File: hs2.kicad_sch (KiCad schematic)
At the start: 55 parts

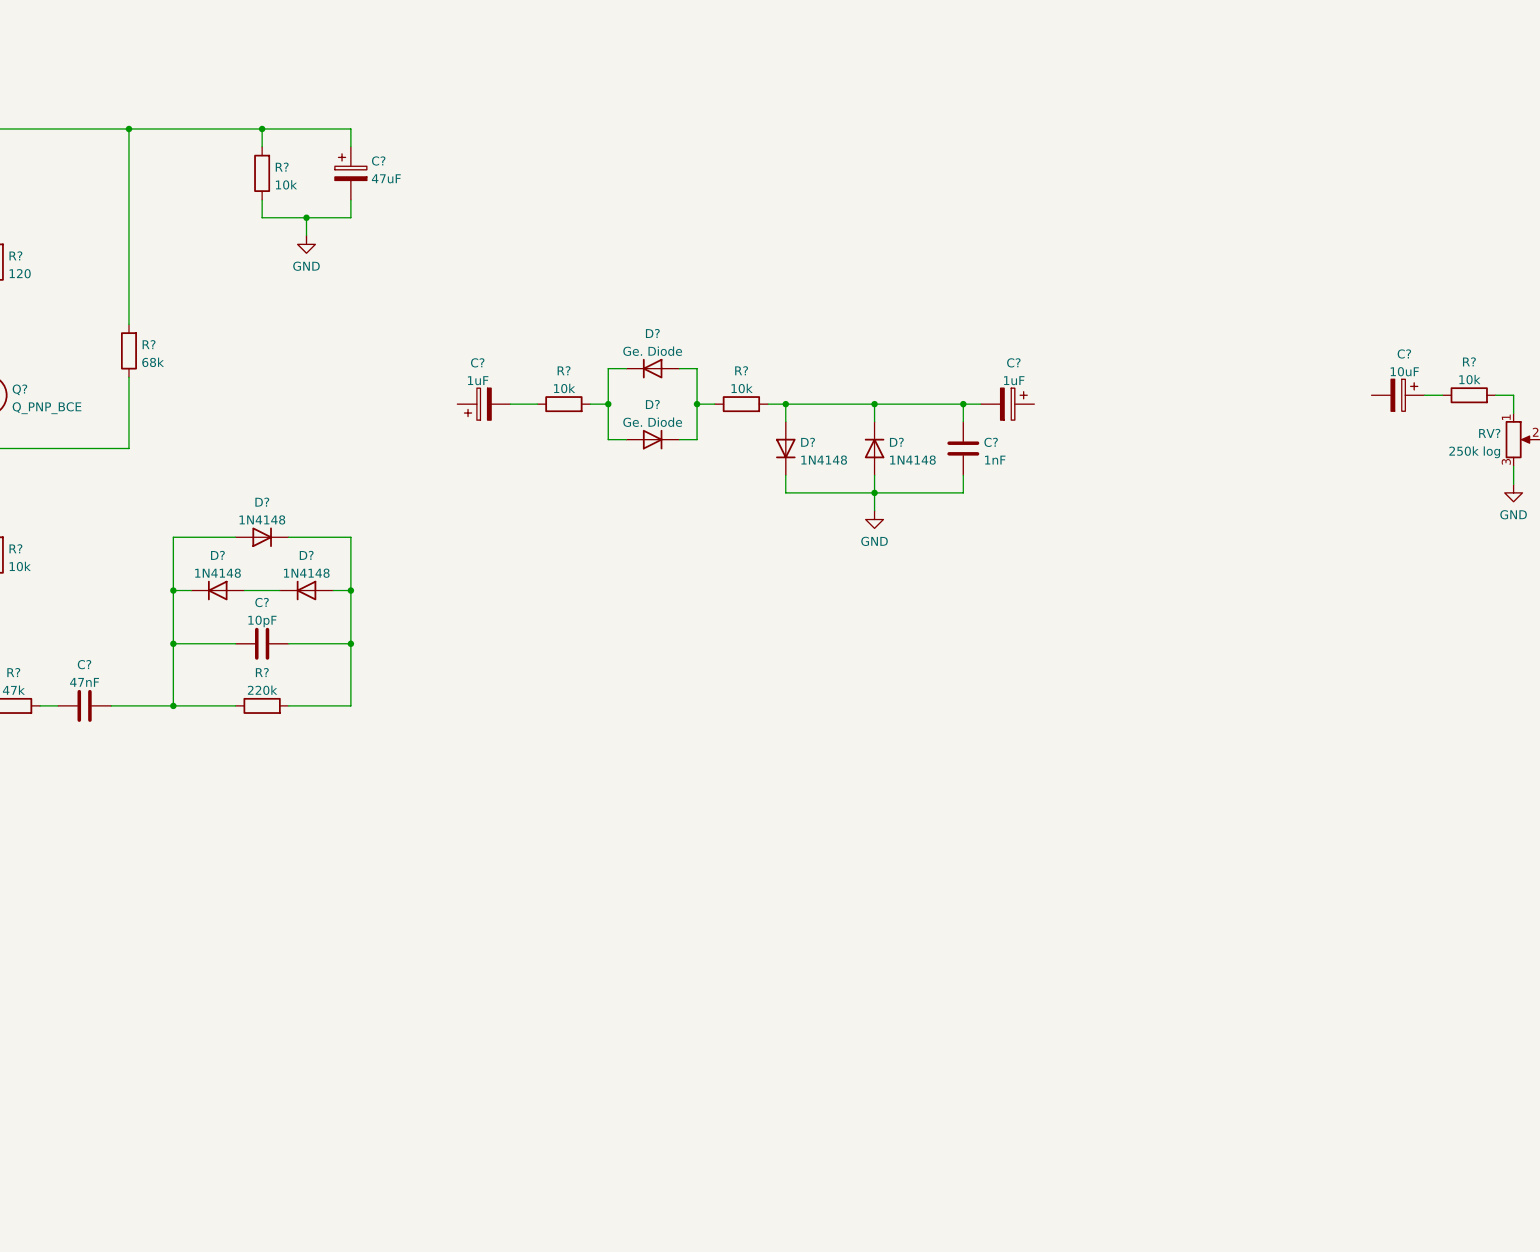
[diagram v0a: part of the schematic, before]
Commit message: Renaming the project
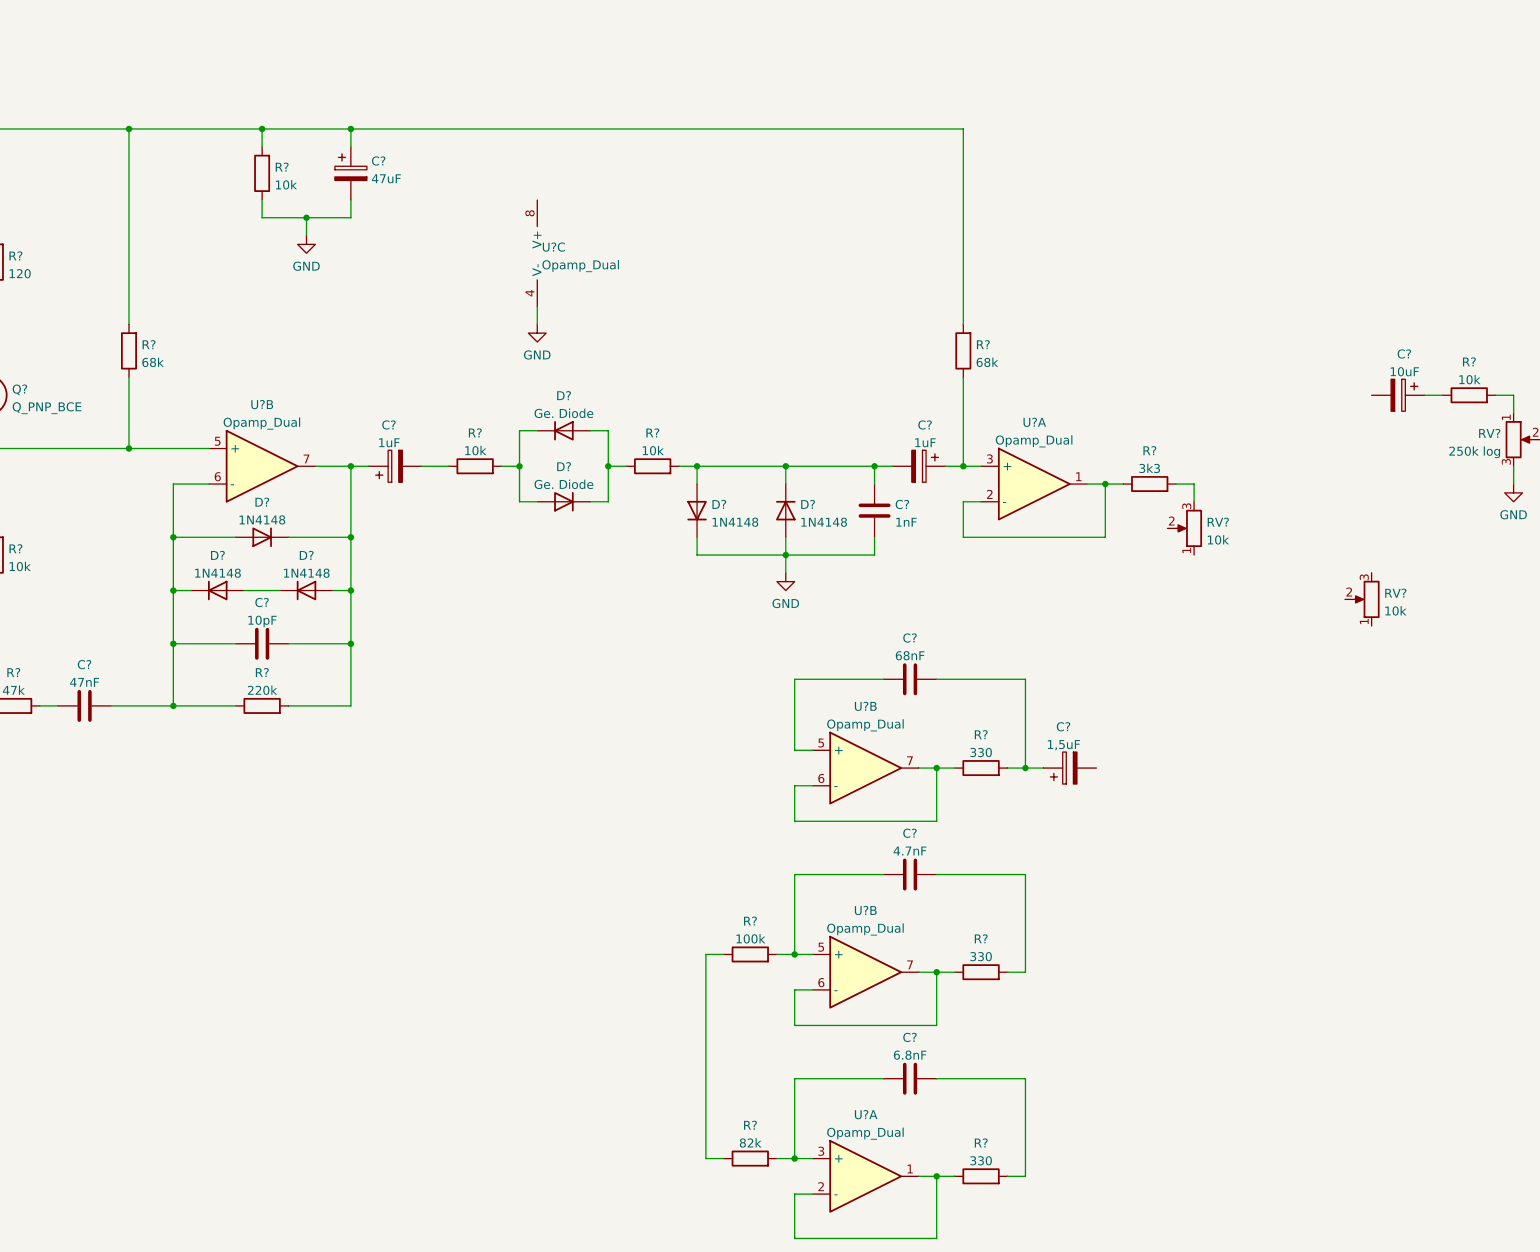
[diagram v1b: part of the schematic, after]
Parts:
- added C?: 68nF, symbol Device:C
- added C?: 1,5uF, symbol Device:C_Polarized
- added C?: 6.8nF, symbol Device:C
- added C?: 4.7nF, symbol Device:C
- added R? (x3): 330, symbol Device:R
- added R?: 3k3, symbol Device:R
- added R?: 82k, symbol Device:R
- added R?: 100k, symbol Device:R
- added R?: 68k, symbol Device:R
- added RV? (x2): 10k, symbol Device:R_Potentiometer
- added U? (x6): Opamp_Dual, symbol Device:Opamp_Dual
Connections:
- net GND: now also U?.4 (V-)
- net at C?.2, D?.1 (K), D?.2 (A)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: now also C?.1, U?.7
- net at C?.1, R?.2, R?.2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: now also R?.2
- net at C?.1, C?.2, D?.1 (K)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: now also U?.6 (-)
- net at C?.2, Q?.2 (C), R?.1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: now also U?.5 (+)
- net at C?.1: now also R?.1, U?.3 (+)
- new net: C?.1, U?.5 (+)
- new net: C?.1, C?.2, R?.2
- new net: C?.1, R?.2, U?.5 (+)
- new net: R?.1, U?.6 (-), U?.7 (x2)
- new net: R?.1, U?.1, U?.2 (-) (x2)
- new net: C?.2, R?.2 (x2)
- new net: R?.2, RV?.3
- new net: R?.1, R?.1
- new net: C?.1, R?.2, U?.3 (+)
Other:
- title: Boss HM-2 -> HS2
- moved on the sheet: C?, D?, R?

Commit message: schematics: Drawing the circuit
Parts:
- removed C?: 68nF, symbol Device:C
- removed C?: 1nF, symbol Device:C
- removed C?: 1,5uF, symbol Device:C_Polarized
- removed C? (x3): 47uF, symbol Device:C_Polarized
- removed C?: 47nF, symbol Device:C
- removed C?: 6.8nF, symbol Device:C
- removed C?: 10uF, symbol Device:C_Polarized
- removed C?: 10pF, symbol Device:C
- removed C?: 4.7nF, symbol Device:C
- removed C? (x2): 1uF, symbol Device:C_Polarized
- removed D? (x5): 1N4148, Diode_THT:D_DO-35_SOD27_P7.62mm_Horizontal, symbol Diode:1N4148
- removed D? (x2): Ge. Diode, symbol Device:D
- removed J?: Conn_01x01, symbol Connector_Generic:Conn_01x01
- removed R? (x3): 330, symbol Device:R
- removed R?: 3k3, symbol Device:R
- removed R?: 82k, symbol Device:R
- removed R?: 1k, symbol Device:R
- removed R? (x2): 68k, symbol Device:R
- removed R?: 150, symbol Device:R
- removed R? (x5): 10k, symbol Device:R
- removed R?: 100k, symbol Device:R
- removed R?: 220k, symbol Device:R
- removed R?: 47k, symbol Device:R
- removed RV? (x2): 10k, symbol Device:R_Potentiometer
- removed RV? (x2): 250k log, symbol Device:R_Potentiometer
- removed U? (x6): Opamp_Dual, symbol Device:Opamp_Dual
- added C?: 47uF, symbol Device:C_Polarized
- added C?: 47n, symbol Device:C
- added C? (x3): 1uF, symbol Device:C_Polarized
- added C?: 47nF, symbol Device:C
- added C?: 1nF, symbol Device:C
- added C?: 150nF, symbol Device:C
- added C?: 470p, symbol Device:C
- added C?: 4.7nF, symbol Device:C
- added C?: 68nF, symbol Device:C
- added C?: 100nF, symbol Device:C
- added C? (x3): 10uF, symbol Device:C_Polarized
- added C?: 100pF, symbol Device:C
- added C?: 6.8nF, symbol Device:C
- added C?: 1.5uF, symbol Device:C_Polarized
- added C?: 100uF, symbol Device:C_Polarized
- added D? (x5): 1N4148, Diode_THT:D_DO-35_SOD27_P7.62mm_Horizontal, symbol Diode:1N4148
- added D?: 1N4001, Diode_THT:D_DO-41_SOD81_P10.16mm_Horizontal, symbol Diode:1N4001
- added D? (x2): DIODE, symbol pspice:DIODE
- added J?: Conn_01x01, symbol Connector_Generic:Conn_01x01
- added R? (x2): 68k, symbol Device:R
- added R?: 470k, symbol Device:R
- added R? (x6): 10k, symbol Device:R
- added R? (x2): 3k3, symbol Device:R
- added R? (x2): 1k, symbol Device:R
- added R? (x3): 100k, symbol Device:R
- added R?: 82k, symbol Device:R
- added R?: 47k, symbol Device:R
- added R? (x4): 330, symbol Device:R
- added R?: 220k, symbol Device:R
- added R?: 150, symbol Device:R
- added RV?: A10k, symbol Device:R_Potentiometer
- added RV? (x2): B50k, symbol Device:R_Potentiometer
- added RV?: C250k, symbol Device:R_Potentiometer
- added U? (x9): Opamp_Dual, symbol Device:Opamp_Dual
- C?: value 47nF -> 100pF
- C?: value 10pF -> 100pF
- R?: value 100k -> 470k
- R?: value 10k -> 22k
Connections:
- net +9V: now also R?.2, R?.2, R?.2, U?.8 (V+), U?.8 (V+), U?.8 (V+)
- net GND: now also C?.2, C?.2, C?.2, C?.2, D?.1 (K), D?.2 (A), D?.2 (A), R?.1, R?.1, R?.1, RV?.1, RV?.2, U?.4 (V-), U?.4 (V-), U?.4 (V-)
- net at C?.1, C?.2, Q?.2 (C)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: now also R?.2
- net at R?.2, R?.2, R?.2: now also C?.1, R?.1
- net 1/2V: now reaches R?.2
- net 1/2V: now also C?.1, R?.1, R?.1, R?.1, R?.1, R?.1, R?.2, R?.2
- net at C?.2, Q?.2 (C), R?.2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: now also R?.1, U?.3 (+)
- new net: R?.2, RV?.3
- new net: C?.2, R?.2
- new net: C?.1, R?.2 (x2)
- new net: C?.2, J?.1 (Pin_1), R?.2
- new net: RV?.1, RV?.1, U?.5 (+)
- new net: C?.1, R?.1, RV?.3, RV?.3, U?.6 (-)
- new net: C?.1, C?.2, R?.2, U?.7
- new net: C?.1, C?.2, D?.1 (K), D?.2 (A), R?.1, U?.2 (-)
- new net: D?.1 (K), D?.2 (A)
- new net: C?.1, R?.2, U?.5 (+)
- new net: C?.1, C?.2, D?.1 (K), D?.2 (A), R?.2
- new net: R?.1, U?.1, U?.2 (-)
- new net: C?.2, R?.2, U?.3 (+)
- new net: D?.1 (K), D?.2 (A), R?.1
- new net: C?.2, R?.1 (x2)
- new net: R?.2, U?.6 (-), U?.7
- new net: C?.1, C?.1, RV?.2
- new net: C?.1, C?.2, R?.2 (x2)
- new net: C?.2, R?.2, U?.2 (-)
- new net: C?.1, C?.2, D?.1 (K), D?.2 (A), R?.2, U?.1
- new net: C?.1, C?.1, R?.2
- new net: C?.1, D?.1 (K), R?.1, R?.1
- new net: C?.2, RV?.2
- new net: R?.1, R?.2
- new net: C?.2, R?.2, U?.6 (-)
- new net: R?.1, RV?.3
- new net: R?.1, U?.1, U?.3 (+)
- new net: C?.2, RV?.1
- new net: C?.1, R?.1
- new net: D?.1 (K), D?.2 (A), R?.2
- new net: R?.1, U?.5 (+), U?.7
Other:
- moved on the sheet: C?, Q?, R?

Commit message: schematics: First version of the schematics
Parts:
- removed Q?: 2SC2240, Package_TO_SOT_THT:TO-92_Inline, symbol Transistor_BJT:2SC1815
- removed Q?: Q_PNP_BCE, symbol Device:Q_PNP_BCE
- added Q2, Q4: 2N3904, Package_TO_SOT_THT:TO-92_Inline, symbol Transistor_BJT:2N3904
- added Q3: 2N3906, Package_TO_SOT_THT:TO-92_Inline, symbol Transistor_BJT:2N3906
- Q1: renamed from Q?; value BF245A -> 2N5457
- gave numbers to parts that had none: 82
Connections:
- net +9V: now also Q4.3 (C)
- net at RV4.2: now also C23.1
- net at C23.2, R34.2: now also Q4.2 (B)
- net at RV2.1, RV3.1, U3.5 (+): now also R30.1
- net at R12.2: now also Q2.1 (E)
- net at C6.2, C8.1, R11.1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: now also Q2.3 (C)
- net at C6.1, R7.2, R8.2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: now also Q2.2 (B)
- net at C10.2, R17.2, R19.2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: now also Q3.1 (E)
- net at C10.1, R14.2, R16.1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: now also Q3.2 (B)
- net at C21.2, R31.2: now also U3.3 (+); no longer U3.2 (-)
- net at R35.2, R36.1: now also Q4.1 (E)
- net at C18.2, R26.2: now also U1.5 (+); no longer U1.6 (-)
- net at R32.1, U3.1: now also U3.2 (-); no longer U3.3 (+)
- net at R18.1: now also Q3.3 (C)
- net at R28.1, U1.7: now also U1.6 (-); no longer U1.5 (+)
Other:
- moved on the sheet: C1, C10, C11, C12, C13, C14, C15, C16, C17, C18, C19, C20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

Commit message: Updating the designators and initial footprint assignment
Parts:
- D5, D6: footprint (none) -> Diode_THT:D_DO-41_SOD81_P10.16mm_Horizontal
- H1, H2, H3, H4: footprint (none) -> MountingHole:MountingHole_3.2mm_M3_Pad_TopBottom
- J1, J2: footprint (none) -> Connector_PinHeader_2.54mm:PinHeader_1x01_P2.54mm_Vertical
- R1, R4: footprint (none) -> Resistor_THT:R_Axial_DIN0207_L6.3mm_D2.5mm_P10.16mm_Horizontal
- R10: renamed from R11; footprint (none) -> Resistor_THT:R_Axial_DIN0207_L6.3mm_D2.5mm_P10.16mm_Horizontal
- R11: renamed from R14; footprint (none) -> Resistor_THT:R_Axial_DIN0207_L6.3mm_D2.5mm_P10.16mm_Horizontal
- R12: renamed from R16; footprint (none) -> Resistor_THT:R_Axial_DIN0207_L6.3mm_D2.5mm_P10.16mm_Horizontal
- R13: renamed from R17; footprint (none) -> Resistor_THT:R_Axial_DIN0207_L6.3mm_D2.5mm_P10.16mm_Horizontal
- R14: renamed from R19; footprint (none) -> Resistor_THT:R_Axial_DIN0207_L6.3mm_D2.5mm_P10.16mm_Horizontal
- R15: renamed from R18; footprint (none) -> Resistor_THT:R_Axial_DIN0207_L6.3mm_D2.5mm_P10.16mm_Horizontal
- R16: renamed from R20; footprint (none) -> Resistor_THT:R_Axial_DIN0207_L6.3mm_D2.5mm_P10.16mm_Horizontal
- R17: renamed from R15; footprint (none) -> Resistor_THT:R_Axial_DIN0207_L6.3mm_D2.5mm_P10.16mm_Horizontal
- R18: renamed from R21; footprint (none) -> Resistor_THT:R_Axial_DIN0207_L6.3mm_D2.5mm_P10.16mm_Horizontal
- R19: renamed from R22; footprint (none) -> Resistor_THT:R_Axial_DIN0207_L6.3mm_D2.5mm_P10.16mm_Horizontal
- R2: renamed from R3; footprint (none) -> Resistor_THT:R_Axial_DIN0207_L6.3mm_D2.5mm_P10.16mm_Horizontal
- R20: renamed from R23; footprint (none) -> Resistor_THT:R_Axial_DIN0207_L6.3mm_D2.5mm_P10.16mm_Horizontal
- R21: renamed from R27; footprint (none) -> Resistor_THT:R_Axial_DIN0207_L6.3mm_D2.5mm_P10.16mm_Horizontal
- R22: renamed from R30; footprint (none) -> Resistor_THT:R_Axial_DIN0207_L6.3mm_D2.5mm_P10.16mm_Horizontal
- R23: renamed from R29; footprint (none) -> Resistor_THT:R_Axial_DIN0207_L6.3mm_D2.5mm_P10.16mm_Horizontal
- R24: renamed from R33; footprint (none) -> Resistor_THT:R_Axial_DIN0207_L6.3mm_D2.5mm_P10.16mm_Horizontal
- R25: renamed from R34; footprint (none) -> Resistor_THT:R_Axial_DIN0207_L6.3mm_D2.5mm_P10.16mm_Horizontal
- R26: renamed from R35; footprint (none) -> Resistor_THT:R_Axial_DIN0207_L6.3mm_D2.5mm_P10.16mm_Horizontal
- R27: renamed from R36; footprint (none) -> Resistor_THT:R_Axial_DIN0207_L6.3mm_D2.5mm_P10.16mm_Horizontal
- R28: renamed from R37; footprint (none) -> Resistor_THT:R_Axial_DIN0207_L6.3mm_D2.5mm_P10.16mm_Horizontal
- R29: renamed from R24; footprint (none) -> Resistor_THT:R_Axial_DIN0207_L6.3mm_D2.5mm_P10.16mm_Horizontal
- R3: renamed from R7; footprint (none) -> Resistor_THT:R_Axial_DIN0207_L6.3mm_D2.5mm_P10.16mm_Horizontal
- R30: renamed from R25; footprint (none) -> Resistor_THT:R_Axial_DIN0207_L6.3mm_D2.5mm_P10.16mm_Horizontal
- R31: renamed from R26; footprint (none) -> Resistor_THT:R_Axial_DIN0207_L6.3mm_D2.5mm_P10.16mm_Horizontal
- R32: renamed from R28; footprint (none) -> Resistor_THT:R_Axial_DIN0207_L6.3mm_D2.5mm_P10.16mm_Horizontal
- R33: renamed from R31; footprint (none) -> Resistor_THT:R_Axial_DIN0207_L6.3mm_D2.5mm_P10.16mm_Horizontal
- R34: renamed from R32; footprint (none) -> Resistor_THT:R_Axial_DIN0207_L6.3mm_D2.5mm_P10.16mm_Horizontal
- R35: renamed from R5; footprint (none) -> Resistor_THT:R_Axial_DIN0207_L6.3mm_D2.5mm_P10.16mm_Horizontal
- R36: renamed from R6; footprint (none) -> Resistor_THT:R_Axial_DIN0207_L6.3mm_D2.5mm_P10.16mm_Horizontal
- R38: renamed from R2; footprint (none) -> Resistor_THT:R_Axial_DIN0207_L6.3mm_D2.5mm_P10.16mm_Horizontal
- R5: renamed from R8; footprint (none) -> Resistor_THT:R_Axial_DIN0207_L6.3mm_D2.5mm_P10.16mm_Horizontal
- R6: renamed from R9; footprint (none) -> Resistor_THT:R_Axial_DIN0207_L6.3mm_D2.5mm_P10.16mm_Horizontal
- R7: renamed from R12; footprint (none) -> Resistor_THT:R_Axial_DIN0207_L6.3mm_D2.5mm_P10.16mm_Horizontal
- R8: renamed from R13; footprint (none) -> Resistor_THT:R_Axial_DIN0207_L6.3mm_D2.5mm_P10.16mm_Horizontal
- R9: renamed from R10; footprint (none) -> Resistor_THT:R_Axial_DIN0207_L6.3mm_D2.5mm_P10.16mm_Horizontal
- U1, U2, U3: footprint (none) -> Package_SIP:SIP-8_19x3mm_P2.54mm
- VR1: renamed from RV1; footprint (none) -> TerminalBlock:TerminalBlock_bornier-3_P5.08mm
- VR2: renamed from RV2; footprint (none) -> TerminalBlock:TerminalBlock_bornier-3_P5.08mm
- VR3: renamed from RV3; footprint (none) -> TerminalBlock:TerminalBlock_bornier-3_P5.08mm
- VR4: renamed from RV4; footprint (none) -> TerminalBlock:TerminalBlock_bornier-3_P5.08mm
- renumbered C12 to C10, C15 to C11, C16 to C12, C19 to C13, C13 to C14, C17 to C15, C20 to C16, C14 to C17, C21 to C19, C3 to C2, C22 to C20, C23 to C21, C24 to C22, C2 to C23, C4 to C24, C6 to C3, C5 to C4, C7 to C5, C8 to C6, C10 to C7, C9 to C8, C11 to C9, D3 to D1, D1 to D3
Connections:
- net at C7.2, R13.2, R14.2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: now also Q3.3 (C); no longer Q3.1 (E)
- net at R15.1: now also Q3.1 (E); no longer Q3.3 (C)

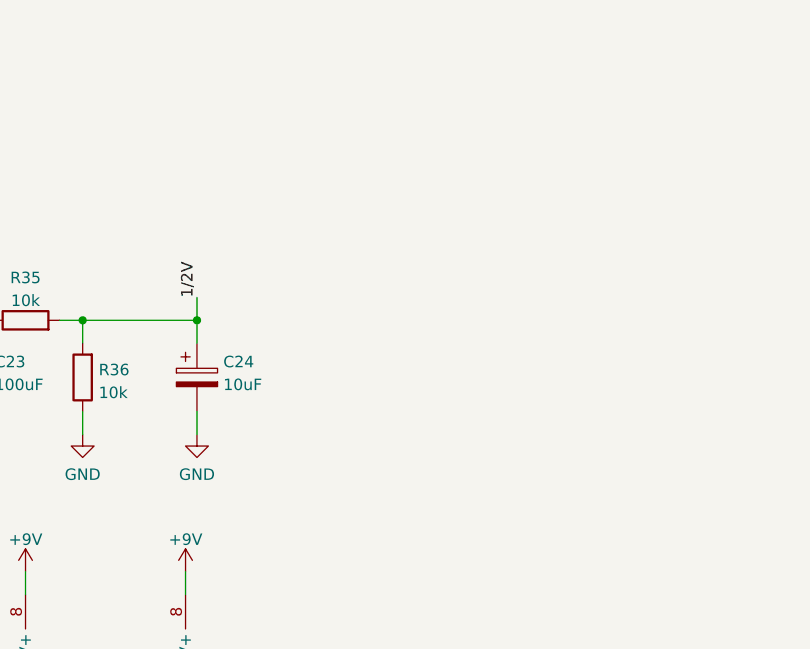
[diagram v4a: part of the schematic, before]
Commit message: layout: Components placement
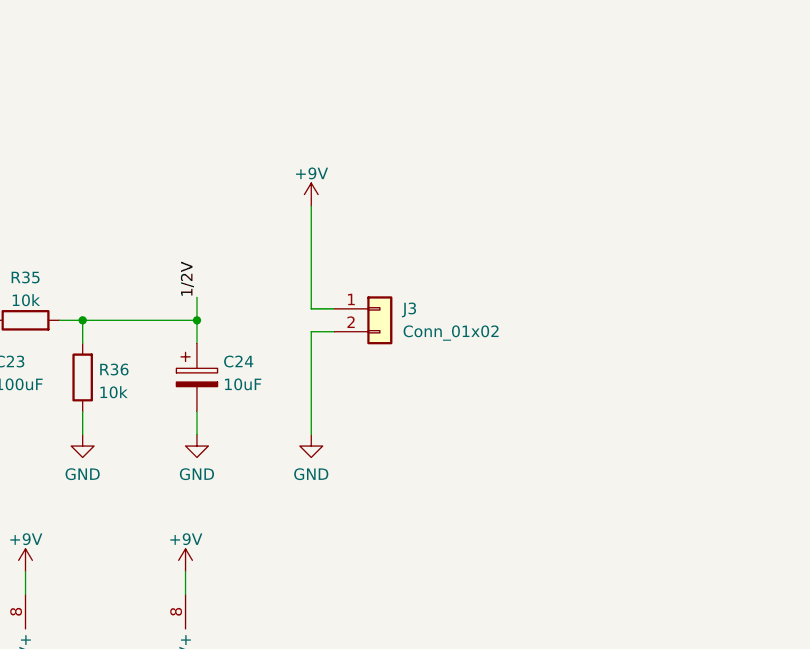
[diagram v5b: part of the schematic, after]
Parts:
- added J3: Conn_01x02, Connector_PinHeader_2.54mm:PinHeader_1x02_P2.54mm_Vertical, symbol Connector_Generic:Conn_01x02
- C1, C13, C15, C16, C17, C18, C19, C2, C21, C3, C6, C7, C8, C9: footprint (none) -> Capacitor_THT:C_Disc_D4.3mm_W1.9mm_P5.00mm
- C10, C11, C12, C14, C20, C22, C23, C24, C4, C5: footprint (none) -> Capacitor_THT:CP_Radial_D5.0mm_P2.50mm
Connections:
- net +9V: now also J3.1 (Pin_1)
- net GND: now also J3.2 (Pin_2)
